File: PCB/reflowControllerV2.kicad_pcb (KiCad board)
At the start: 4 copper layers, 43 x 89 mm, 100 parts, among them J1 CN4, J10 NEXTION_OB, J11 PWR, J12 A-1JB, J2 SSR2, J3 SSR1, J4 FAN1, J5 FAN2, J6 T1, J7 T2, J8 SWD, J9 NEXTION_FRONT, Q1 2N3904, Q2 2N3904, Q3 2N3904, Q4 2N3904, Q5 2N3904, SW1 B3F-4055, U1 918-468K2029E50001, U10 ZD24C128A, U2 918-468K2029E50001, U3 AMS1117-3.3, U4 STM32WBxx_QFN48, U5 USBLC6-2SC6, U6 USBLC6-2SC6, U7 CH340G, U8 MAX31855KASA, U9 MAX31855KASA, Y1 NX2016_32MHz, Y2 NX2012_32K768Hz, Y3 12M

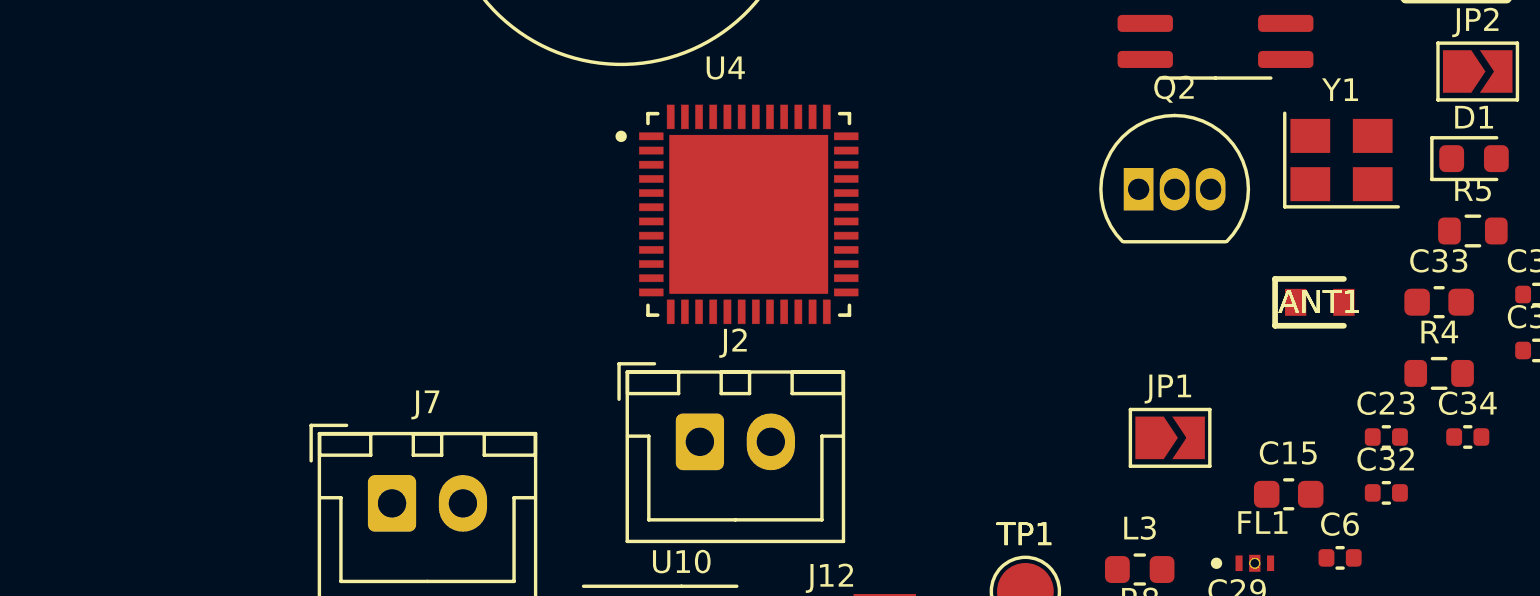
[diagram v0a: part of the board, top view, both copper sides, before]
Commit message: PCB antenna removed
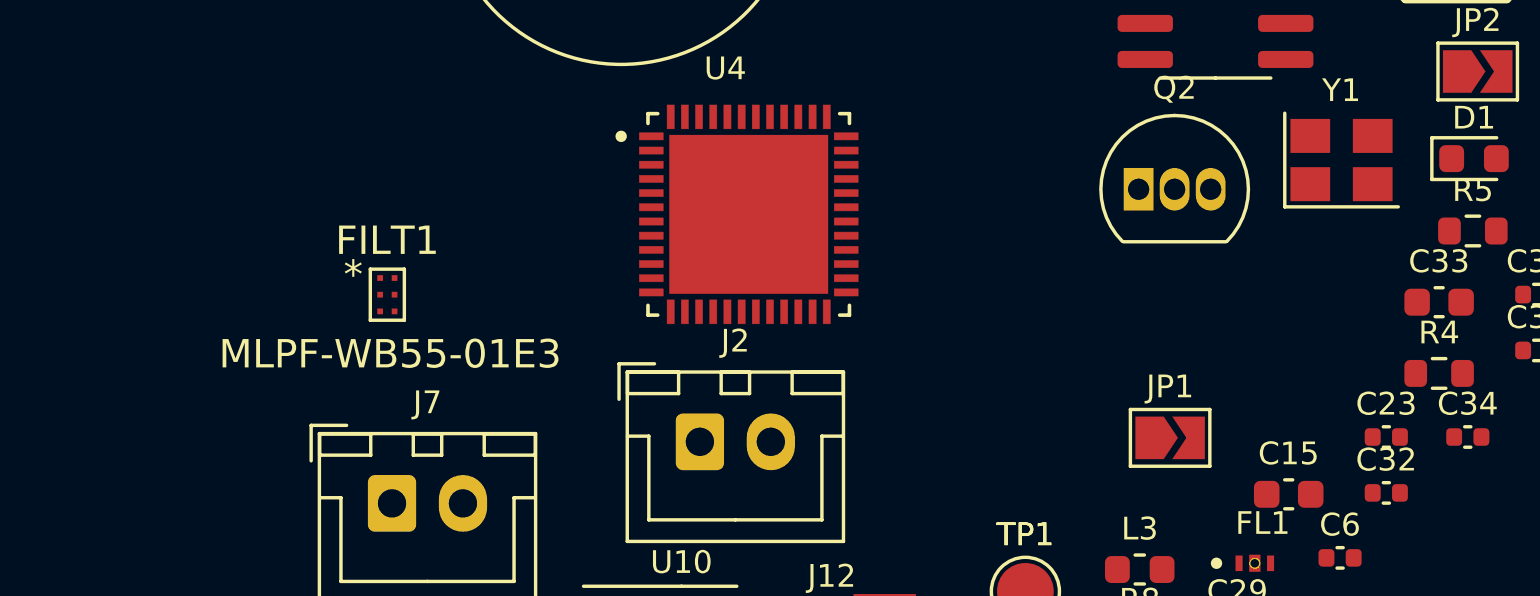
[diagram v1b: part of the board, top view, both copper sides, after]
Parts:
- removed ANT1: 2450AT14A0100T, footprints:ANTC1608X40N
- added FILT1: MLPF-WB55-01E3, footprints:MLPF-WB55-01E3, F.Cu at (-34.9, -14.3)
- C26: value 0.8p -> NF
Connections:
- U4 pad 21: Net-(C20-Pad2) -> Net-(U4-Pad21)
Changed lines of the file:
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@@
   (net 20 "Net-(C30-Pad2)")
   (net 21 "Net-(C31-Pad2)")
-  (net 22 "Net-(ANT1-Pad1)")
+  (net 22 "Net-(C32-Pad2)")
   (net 23 "Net-(C34-Pad2)")
   (net 24 "Net-(C36-Pad2)")
@@
   (net 76 "/SPI_SO")
   (net 77 "/T2_CS")
-  (net 78 "unconnected-(ANT1-Pad2)")
+  (net 78 "Net-(U4-Pad21)")
   (net 79 "Net-(J12-PadGND1)")
   (net 80 "unconnected-(U1-PadA5)")
@@
       (net 19 "Net-(C24-Pad2)") (pintype "passive"))
     (pad "2" smd roundrect (at 0.485 0) (size 0.59 0.64) (layers "F.Cu" "F.Paste" "F.Mask") (roundrect_rratio 0.25)
-      (net 22 "Net-(ANT1-Pad1)") (pintype "passive"))
+      (net 22 "Net-(C32-Pad2)") (pintype "passive"))
     (model "${KICAD6_3DMODEL_DIR}/Inductor_SMD.3dshapes/L_0402_1005Metric.wrl"
       (offset (xyz 0 0 0))
@@
     )
   )
-  (footprint "footprints:ANTC1608X40N" (layer "F.Cu")
-    (at -2 -14)
-    (descr "2450AT14A0100T-1")
-    (tags "Antenna")
-    (property "Description" "Antennas SMALL AREA 2.4G ANT")
-    (property "Height" "0.4")
-    (property "Manufacturer_Name" "JOHANSON TECHNOLOGY")
-    (property "Manufacturer_Part_Number" "2450AT14A0100T")
-    (property "Mouser Part Number" "609-2450AT14A0100T")
-    (property "Mouser Price/Stock" "https://www.mouser.co.uk/ProductDetail/Johanson-Technology/2450AT14A0100T?qs=YCa%2FAAYMW01CU618jkZ%252BCw%3D%3D")
-    (property "Sheetfile" "reflowControllerV2.kicad_sch")
-    (property "Sheetname" "")
-    (attr smd)
-    (fp_text reference "ANT1" (at 0 0) (layer "F.SilkS")
-      (effects (font (size 0.8 0.8) (thickness 0.12)))
-    )
-    (fp_text value "2450AT14A0100T" (at 0 0) (layer "F.SilkS") hide
-      (effects (font (size 1.27 1.27) (thickness 0.254)))
-    )
-    (fp_text user "${REFERENCE}" (at 0 0) (layer "F.SilkS")
-      (effects (font (size 0.8 0.8) (thickness 0.12)))
-    )
-    (fp_line (start -1.575 -0.825) (end -1.575 0.825) (layer "F.SilkS") (width 0.2))
-    (fp_line (start -1.575 0.825) (end 0.85 0.825) (layer "F.SilkS") (width 0.2))
-    (fp_line (start 0.85 -0.825) (end -1.575 -0.825) (layer "F.SilkS") (width 0.2))
-    (fp_line (start -1.675 -0.925) (end 1.675 -0.925) (layer "F.CrtYd") (width 0.05))
-    (fp_line (start -1.675 0.925) (end -1.675 -0.925) (layer "F.CrtYd") (width 0.05))
-    (fp_line (start 1.675 0.925) (end -1.675 0.925) (layer "F.CrtYd") (width 0.05))
-    (fp_line (start 1.675 -0.925) (end 1.675 0.925) (layer "F.CrtYd") (width 0.05))
-    (fp_line (start -0.8 0.4) (end -0.8 -0.4) (layer "F.Fab") (width 0.1))
-    (fp_line (start 0.8 -0.4) (end 0.8 0.4) (layer "F.Fab") (width 0.1))
-    (fp_line (start -0.8 -0.4) (end 0.8 -0.4) (layer "F.Fab") (width 0.1))
-    (fp_line (start 0.8 0.4) (end -0.8 0.4) (layer "F.Fab") (width 0.1))
-    (fp_line (start -0.8 -0.025) (end -0.425 -0.4) (layer "F.Fab") (width 0.1))
-    (pad "1" smd rect locked (at -0.85 0) (size 0.75 0.95) (layers "F.Cu" "F.Paste" "F.Mask")
-      (net 22 "Net-(ANT1-Pad1)") (pinfunction "FEED") (pintype "input"))
-    (pad "2" smd rect locked (at 0.85 0) (size 0.75 0.95) (layers "F.Cu" "F.Paste" "F.Mask")
-      (net 78 "unconnected-(ANT1-Pad2)") (pinfunction "NC") (pintype "no_connect"))
-    (model "C:\\Users\\lukas\\Desktop\\Projects\\KICAD\\SamacSys_Parts.3dshapes\\2450AT14A0100T.stp"
-      (offset (xyz 0 0 0))
-      (scale (xyz 1 1 1))
-      (rotate (xyz 0 0 0))
-    )
-  )
   (footprint "Connector_JST:JST_XH_B2B-XH-A_1x02_P2.50mm_Vertical" (layer "F.Cu")
     (at 1.255 -39.915)
@@
       (net 4 "GND") (pintype "passive"))
     (pad "2" smd roundrect (at 0.48 0) (size 0.56 0.62) (layers "F.Cu" "F.Paste" "F.Mask") (roundrect_rratio 0.25)
-      (net 22 "Net-(ANT1-Pad1)") (pintype "passive"))
+      (net 22 "Net-(C32-Pad2)") (pintype "passive"))
     (model "${KICAD6_3DMODEL_DIR}/Capacitor_SMD.3dshapes/C_0402_1005Metric.wrl"
       (offset (xyz 0 0 0))
@@
       (effects (font (size 0.8 0.8) (thickness 0.12)))
     )
-    (fp_text value "0.8p" (at 0 1.16) (layer "F.Fab")
+    (fp_text value "NF" (at 0 1.16) (layer "F.Fab")
       (effects (font (size 1 1) (thickness 0.15)))
     )
@@
     )
   )
+  (footprint "footprints:MLPF-WB55-01E3" (layer "F.Cu")
+    (at -34.86 -14.27)
+    (property "Sheetfile" "reflowControllerV2.kicad_sch")
+    (property "Sheetname" "")
+    (attr through_hole)
+    (fp_text reference "FILT1" (at 0 -1.9) (layer "F.SilkS")
+      (effects (font (size 1 1) (thickness 0.15)))
+    )
+    (fp_text value "MLPF-WB55-01E3" (at 0.1 2.1) (layer "F.SilkS")
+      (effects (font (size 1 1) (thickness 0.15)))
+    )
+    (fp_text user "*" (at -1.2 -0.7) (layer "F.SilkS")
+      (effects (font (size 1 1) (thickness 0.15)))
+    )
+    (fp_text user "*" (at -1.2 -0.7) (layer "F.Fab")
+      (effects (font (size 1 1) (thickness 0.15)))
+    )
+    (fp_line (start -0.6 0.9) (end 0.6 0.9) (layer "F.SilkS") (width 0.12))
+    (fp_line (start 0.6 -0.9) (end -0.6 -0.9) (layer "F.SilkS") (width 0.12))
+    (fp_line (start -0.6 -0.9) (end -0.6 0.9) (layer "F.SilkS") (width 0.12))
+    (fp_line (start 0.6 0.9) (end 0.6 -0.9) (layer "F.SilkS") (width 0.12))
+    (fp_line (start -0.762 -1.0668) (end 0.762 -1.0668) (layer "F.CrtYd") (width 0.05))
+    (fp_line (start 0.762 -0.9426) (end 0.762 -0.9426) (layer "F.CrtYd") (width 0.05))
+    (fp_line (start 0.762 0.9426) (end 0.762 0.9426) (layer "F.CrtYd") (width 0.05))
+    (fp_line (start 0.762 -0.9426) (end 0.762 -0.9426) (layer "F.CrtYd") (width 0.05))
+    (fp_line (start 0.762 0.9426) (end 0.762 1.0668) (layer "F.CrtYd") (width 0.05))
+    (fp_line (start -0.762 -1.0668) (end -0.762 1.0668) (layer "F.CrtYd") (width 0.05))
+    (fp_line (start -0.762 -1.0668) (end 0.762 -1.0668) (layer "F.CrtYd") (width 0.05))
+    (fp_line (start 0.762 0.9426) (end 0.762 0.9426) (layer "F.CrtYd") (width 0.05))
+    (fp_line (start 0.762 0.9426) (end 0.762 1.0668) (layer "F.CrtYd") (width 0.05))
+    (fp_line (start 0.762 1.0668) (end -0.762 1.0668) (layer "F.CrtYd") (width 0.05))
+    (fp_line (start 0.762 -0.9426) (end 0.762 0.9426) (layer "F.CrtYd") (width 0.05))
+    (fp_line (start 0.762 -1.0668) (end 0.762 -0.9426) (layer "F.CrtYd") (width 0.05))
+    (fp_line (start 0.762 1.0668) (end -0.762 1.0668) (layer "F.CrtYd") (width 0.05))
+    (fp_line (start 0.762 -1.0668) (end 0.762 -0.9426) (layer "F.CrtYd") (width 0.05))
+    (fp_line (start 0.762 -0.9426) (end 0.762 0.9426) (layer "F.CrtYd") (width 0.05))
+    (fp_line (start -0.508 -0.8128) (end -0.508 0.8128) (layer "F.Fab") (width 0.1))
+    (fp_line (start -0.508 0.8128) (end 0.508 0.8128) (layer "F.Fab") (width 0.1))
+    (fp_line (start 0.508 -0.8128) (end -0.508 -0.8128) (layer "F.Fab") (width 0.1))
+    (fp_line (start 0.508 0.8128) (end 0.508 -0.8128) (layer "F.Fab") (width 0.1))
+    (pad "1" smd rect (at -0.254 -0.586999) (size 0.2032 0.2032) (layers "F.Cu" "F.Paste" "F.Mask")
+      (net 18 "Net-(C24-Pad1)") (pinfunction "OUT") (pintype "output"))
+    (pad "2" smd rect (at -0.254 0) (size 0.2032 0.2032) (layers "F.Cu" "F.Paste" "F.Mask")
+      (net 4 "GND") (pinfunction "GND") (pintype "power_in"))
+    (pad "3" smd rect (at -0.254 0.586999) (size 0.2032 0.2032) (layers "F.Cu" "F.Paste" "F.Mask")
+      (net 78 "Net-(U4-Pad21)") (pinfunction "IN") (pintype "input"))
+    (pad "4" smd rect (at 0.254 0.586999) (size 0.2032 0.2032) (layers "F.Cu" "F.Paste" "F.Mask")
+      (net 4 "GND") (pinfunction "GND") (pintype "power_in"))
+    (pad "5" smd rect (at 0.254 0) (size 0.2032 0.2032) (layers "F.Cu" "F.Paste" "F.Mask")
+      (net 4 "GND") (pinfunction "GND") (pintype "power_in"))
+    (pad "6" smd rect (at 0.254 -0.586999) (size 0.2032 0.2032) (layers "F.Cu" "F.Paste" "F.Mask")
+      (net 4 "GND") (pinfunction "GND") (pintype "power_in"))
+  )
   (footprint "Capacitor_SMD:C_0603_1608Metric" (layer "F.Cu")
     (at 30 48 180)
@@
       (net 1 "+3V3") (pinfunction "VDD/VDDT") (pintype "power_in"))
     (pad "21" smd roundrect locked (at 1.25 3.435 90) (size 0.86 0.27) (layers "F.Cu" "F.Paste" "F.Mask") (roundrect_rratio 0.03)
-      (net 16 "Net-(C20-Pad2)") (pinfunction "RF1") (pintype "output"))
+      (net 78 "Net-(U4-Pad21)") (pinfunction "RF1") (pintype "output"))
     (pad "22" smd roundrect locked (at 1.75 3.435 90) (size 0.86 0.27) (layers "F.Cu" "F.Paste" "F.Mask") (roundrect_rratio 0.03)
       (net 4 "GND") (pinfunction "RF0") (pintype "power_in"))

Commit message: Further component placing
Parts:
- removed FL1: LFB182G45CGFD436, footprints:FIL_LFB182G45CGFD436
- added ANT1: M830520, footprints:M830520, F.Cu at (2.00, 57.8)
- J1: footprint Connector_PinHeader_2.54mm:PinHeader_1x04_P2.54mm_Vertical -> Connector_PinHeader_1.00mm:PinHeader_1x04_P1.00mm_Vertical
- JP1, JP2: footprint Jumper:SolderJumper-2_P1.3mm_Open_TrianglePad1.0x1.5mm -> Resistor_SMD:R_0603_1608Metric
- R6: moved to B.Cu
- Y1: footprint Crystal:Crystal_SMD_3225-4Pin_3.2x2.5mm -> Crystal:Crystal_SMD_2016-4Pin_2.0x1.6mm
- moved J8 114.2 mm to (39.1, 35.5), turned to 90 degrees
- moved J1 107.2 mm to (30.4, 56.6)
- moved J4 105.5 mm to (11.3, 65.1)
- moved C18 97.0 mm to (16.5, 56.0)
- moved C19 93.2 mm to (16.5, 55.0)
- moved L2 93.1 mm to (9.90, 54.4)
- moved C28 90.1 mm to (28.0, 56.8)
- moved C27 87.5 mm to (16.5, 51.6), turned to 180 degrees
- moved JP2 85.1 mm to (26.3, 59.9), turned to 180 degrees
- moved J5 84.8 mm to (11.3, 72.1)
- moved FILT1 84.7 mm to (16.4, 53.1), turned to 90 degrees
- moved U4 82.4 mm to (22.6, 52.1), turned to -90 degrees
- moved Y1 80.3 mm to (19.1, 58.7), turned to 90 degrees
- moved C26 79.6 mm to (11.4, 54.9), turned to 90 degrees
- moved C25 78.5 mm to (25.3, 58.1), turned to 90 degrees
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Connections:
- J6 pad 1: /T1+ -> /T1-
- J6 pad 2: /T1- -> /T1+
- J7 pad 1: /T2+ -> /T2-
- J7 pad 2: /T2- -> /T2+

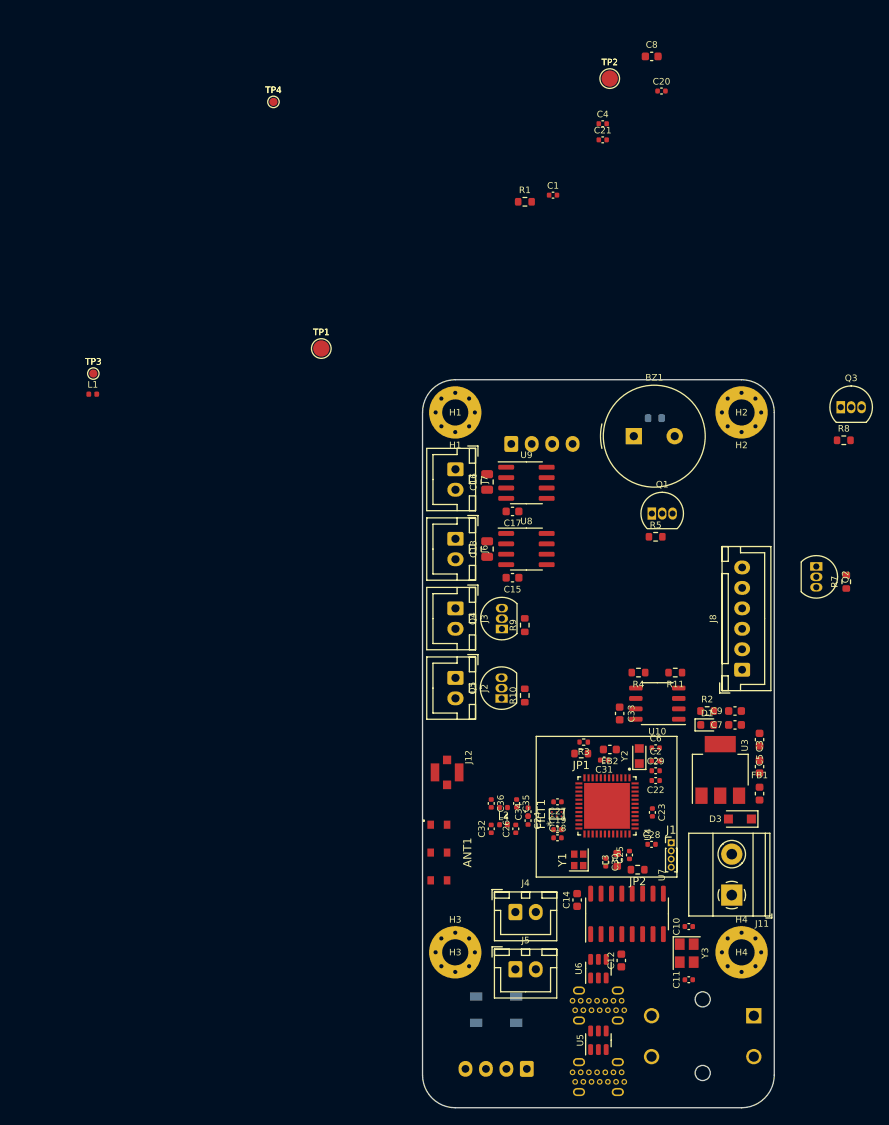
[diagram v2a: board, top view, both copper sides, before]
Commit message: RF Routing, Guard Ring, component placing, switching to mosfets
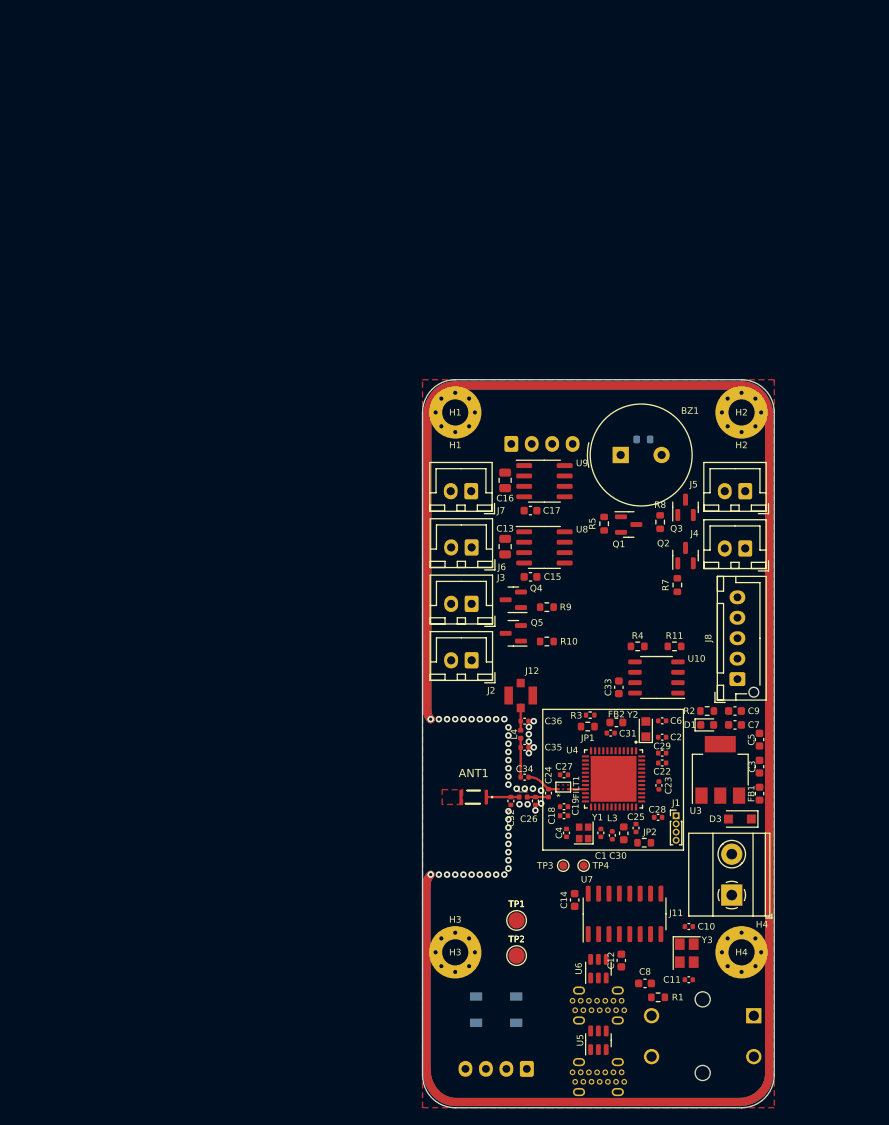
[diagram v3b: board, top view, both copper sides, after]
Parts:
- removed C20: 0.8p, Capacitor_SMD:C_0402_1005Metric
- removed C21: NF, Capacitor_SMD:C_0402_1005Metric
- removed L1: 0R, Inductor_SMD:L_0402_1005Metric
- ANT1: value M830520 -> ANT3216LL00R2400A; footprint footprints:M830520 -> footprints:ANT3216LL00R2400A
- J8: footprint Connector_JST:JST_XH_B6B-XH-A_1x06_P2.50mm_Vertical -> Connector_JST:JST_XH_B5B-XH-AM_1x05_P2.50mm_Vertical
- Q1, Q2, Q3, Q4, Q5: value 2N3904 -> BSS316NH6327; footprint Package_TO_SOT_THT:TO-92_Inline -> Package_TO_SOT_SMD:SOT-23
- moved C8 113.3 mm to (27.2, 73.8)
- moved TP2 107.8 mm to (11.5, 70.4)
- moved TP4 100.8 mm to (19.7, 59.4)
- moved R1 98.6 mm to (28.8, 75.5), turned to 180 degrees
- moved C4 86.8 mm to (17.6, 55.4), turned to -90 degrees
- moved TP3 83.2 mm to (17.2, 59.4)
- moved C1 78.2 mm to (21.8, 55.4), turned to 90 degrees
- moved TP1 73.9 mm to (11.5, 66.1)
- moved J5 64.9 mm to (39.5, 13.6), turned to 180 degrees
- moved J4 52.6 mm to (39.5, 20.6), turned to 180 degrees
- moved R8 24.6 mm to (29.1, 17.4), turned to 90 degrees
- moved Q3 22.6 mm to (32.1, 15.6), turned to 90 degrees
- moved R7 20.7 mm to (31.1, 25.1)
- moved Q2 16.0 mm to (32.1, 21.5), turned to 90 degrees
- moved J12 13.0 mm to (12.0, 38.6)
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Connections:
- ANT1 pad 1: Net-(ANT1-Pad1) -> Net-(C32-Pad2)
- ANT1 pad 2: Net-(ANT1-Pad1) -> /ANT_NC
- C32 pad 2: Net-(ANT1-Pad1) -> Net-(C32-Pad2)
- J12 pad GND1: Net-(J12-PadGND1) -> GND
- J12 pad GND2: Net-(J12-PadGND1) -> GND
- J12 pad OPTIONAL_GND: Net-(J12-PadGND1) -> GND
- J8 pad 5: /SWO -> GND
- L2 pad 2: Net-(ANT1-Pad1) -> Net-(C32-Pad2)
- Q1 pad 1: GND -> Net-(R5-Pad2)
- Q1 pad 2: Net-(Q1-Pad2) -> GND
- Q2 pad 1: GND -> Net-(R7-Pad2)
- Q2 pad 2: Net-(Q2-Pad2) -> GND
- Q3 pad 1: GND -> Net-(R8-Pad2)
- Q3 pad 2: Net-(Q3-Pad2) -> GND
- Q4 pad 1: GND -> Net-(R9-Pad2)
- Q4 pad 2: Net-(Q4-Pad2) -> GND
- Q5 pad 1: GND -> Net-(R10-Pad2)
- Q5 pad 2: Net-(Q5-Pad2) -> GND
- R10 pad 2: Net-(Q5-Pad2) -> Net-(R10-Pad2)
- R5 pad 2: Net-(Q1-Pad2) -> Net-(R5-Pad2)
- R7 pad 2: Net-(Q2-Pad2) -> Net-(R7-Pad2)
- R8 pad 2: Net-(Q3-Pad2) -> Net-(R8-Pad2)
- R9 pad 2: Net-(Q4-Pad2) -> Net-(R9-Pad2)
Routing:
- net GND: track 0.00 -> 467.6 mm, vias 0 -> 50
- net Net-(C34-Pad2): track 0.00 -> 4.76 mm
- net Net-(C24-Pad1): track 0.00 -> 4.17 mm
- net Net-(C32-Pad2): track 0.00 -> 4.01 mm
- net Net-(C36-Pad2): track 0.00 -> 3.13 mm
- net Net-(C24-Pad2): track 0.00 -> 2.62 mm
- net Net-(FILT1-Pad3): track 0.00 -> 2.13 mm
- added copper zone on F.Cu, net /ANT_NC
- added copper zone on F.Cu, net GND
